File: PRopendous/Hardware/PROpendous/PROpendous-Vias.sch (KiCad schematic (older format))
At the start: 331 parts

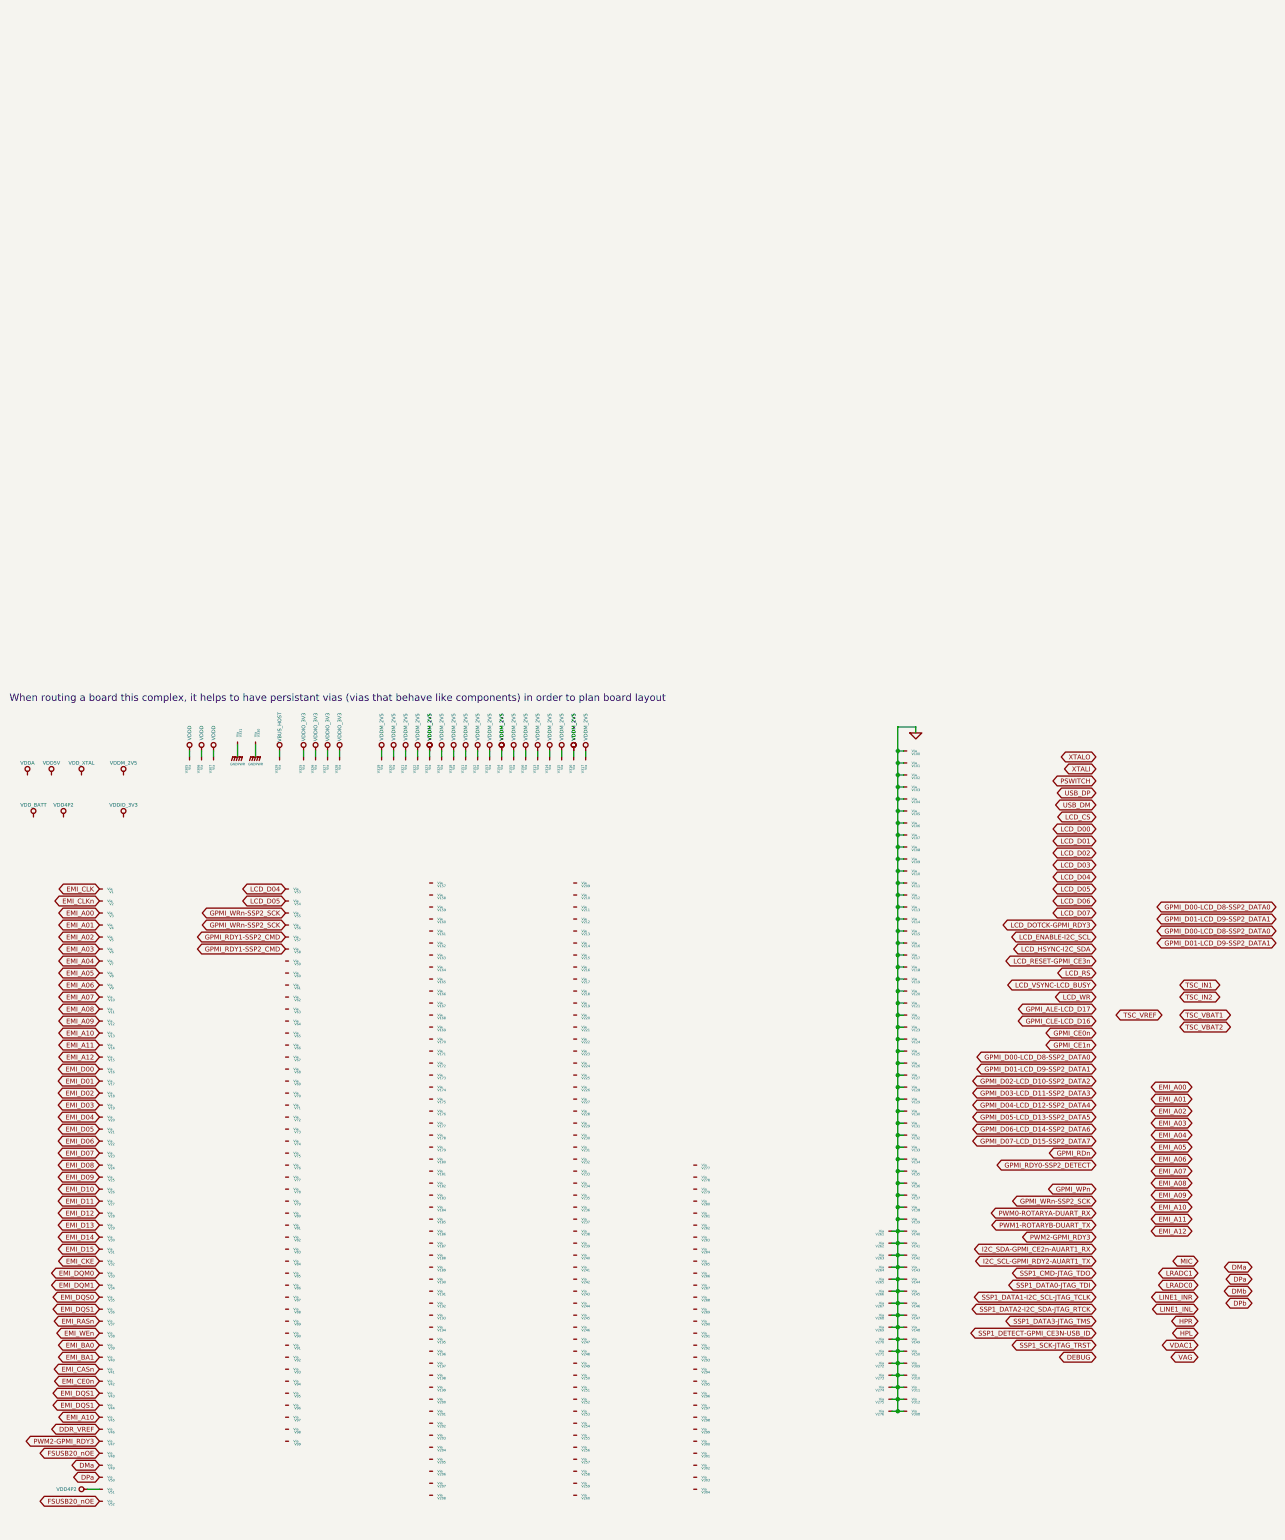
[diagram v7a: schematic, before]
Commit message: First revision of i.MX233-based PROpendous board is complete.
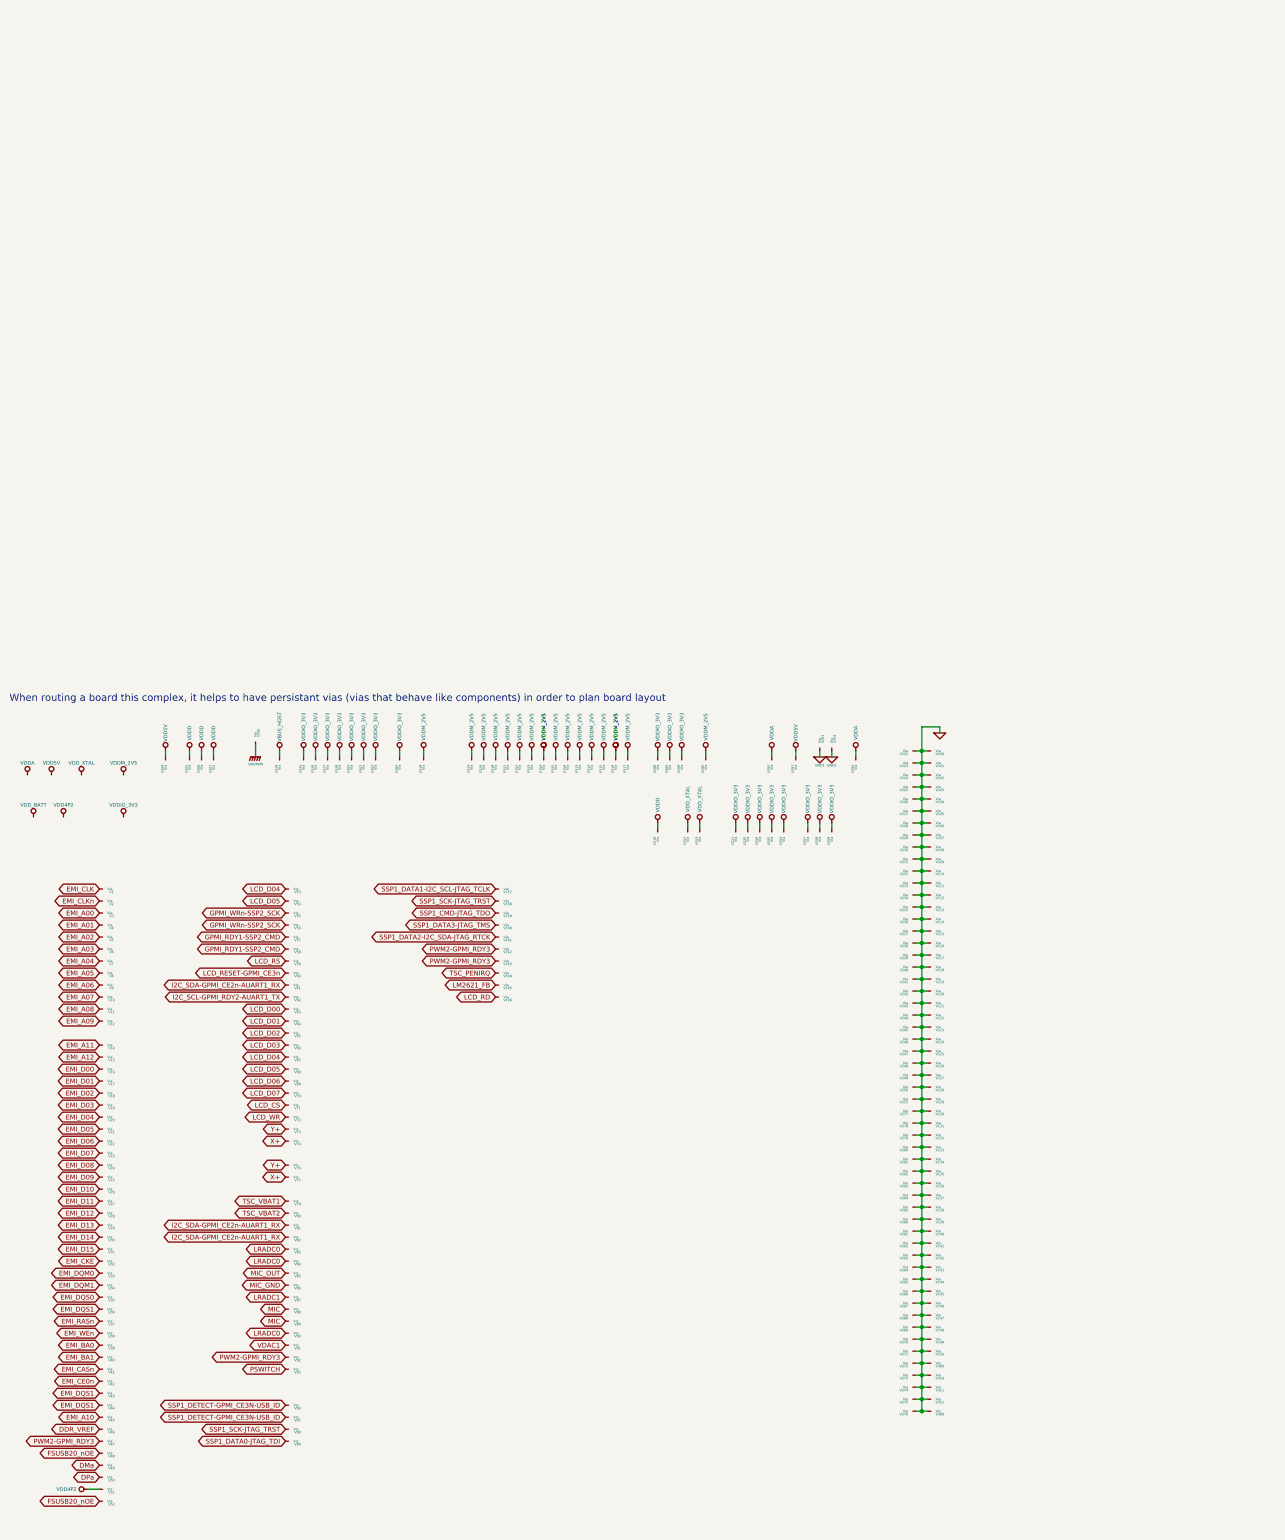
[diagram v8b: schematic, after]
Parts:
- removed V13, V167, V168, V169, V170, V171, V172, V173, V174, V175, V176, V177, V178, V179, V180, V181, V182, V183, V184, V185, V186, V187, V188, V189, V190, V191, V192, V193, V194, V195, V196, V197, V198, V199, V200, V201, V202, V203, V204, V205, V206, V207, V208, V209, V210, V211, V212, V213, V214, V215, V216, V217, V218, V287, V288, V289, V295, V296, V320, V321, V322, V331, V75, V78, V94, V95: VIA, symbol VIA
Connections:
- net GND: now also V222.1 (Via), V223.1 (Via), V224.1 (Via), V225.1 (Via), V226.1 (Via), V227.1 (Via), V228.1 (Via), V229.1 (Via), V230.1 (Via), V231.1 (Via), V232.1 (Via), V233.1 (Via), V234.1 (Via), V235.1 (Via), V236.1 (Via), V237.1 (Via), V238.1 (Via), V239.1 (Via), V240.1 (Via), V241.1 (Via), V242.1 (Via), V243.1 (Via), V244.1 (Via), V245.1 (Via), V246.1 (Via), V247.1 (Via), V248.1 (Via), V249.1 (Via), V250.1 (Via), V251.1 (Via), V277.1 (Via), V278.1 (Via), V279.1 (Via), V280.1 (Via), V281.1 (Via), V282.1 (Via), V283.1 (Via), V284.1 (Via), V285.1 (Via), V286.1 (Via)
- net I2C_SCL-GPMI_RDY2-AUART1_TX: now also V62.1 (Via)
- net I2C_SDA-GPMI_CE2n-AUART1_RX: now also V61.1 (Via), V81.1 (Via), V82.1 (Via)
- net LCD_CS: now also V71.1 (Via)
- net LCD_D00: now also V63.1 (Via)
- net LCD_D01: now also V64.1 (Via)
- net LCD_D02: now also V65.1 (Via)
- net LCD_D03: now also V66.1 (Via)
- net LCD_D04: now also V67.1 (Via)
- net LCD_D05: now also V68.1 (Via)
- net LCD_D06: now also V69.1 (Via)
- net LCD_D07: now also V70.1 (Via)
- net LCD_RESET-GPMI_CE3n: now also V60.1 (Via)
- net LCD_RS: now also V59.1 (Via)
- net LCD_WR: now also V72.1 (Via)
- net LRADC0: now also V83.1 (Via), V84.1 (Via), V90.1 (Via)
- net LRADC1: now also V87.1 (Via)
- net MIC: now also V88.1 (Via), V89.1 (Via)
- net PSWITCH: now also V93.1 (Via)
- net PWM2-GPMI_RDY3: now also V162.1 (Via), V163.1 (Via), V92.1 (Via)
- net SSP1_CMD-JTAG_TDO: now also V159.1 (Via)
- net SSP1_DATA0-JTAG_TDI: now also V99.1 (Via)
- net SSP1_DATA1-I2C_SCL-JTAG_TCLK: now also V157.1 (Via)
- net SSP1_DATA2-I2C_SDA-JTAG_RTCK: now also V161.1 (Via)
- net SSP1_DATA3-JTAG_TMS: now also V160.1 (Via)
- net SSP1_DETECT-GPMI_CE3N-USB_ID: now also V96.1 (Via), V97.1 (Via)
- net SSP1_SCK-JTAG_TRST: now also V158.1 (Via), V98.1 (Via)
- net TSC_VBAT1: now also V79.1 (Via)
- net TSC_VBAT2: now also V80.1 (Via)
- net VDAC1: now also V91.1 (Via)
- net VDD5V: now also V297.1 (Via), V304.1 (Via)
- net VDDA: now also V292.1 (Via), V294.1 (Via)
- net VDDD: now also V219.1 (Via)
- net VDDIO_3V3: now also V220.1 (Via), V221.1 (Via), V254.1 (Via), V255.1 (Via), V256.1 (Via), V257.1 (Via), V258.1 (Via), V259.1 (Via), V260.1 (Via), V298.1 (Via), V299.1 (Via), V300.1 (Via), V301.1 (Via), V302.1 (Via), V303.1 (Via)
- net VDDM_2V5: now also V290.1 (Via)
- net VDD_XTAL: now also V252.1 (Via), V253.1 (Via)
- net MIC_OUT: now reaches V85.1 (Via)
- net MIC_GND: now reaches V86.1 (Via)
- net Y+: now reaches V73.1 (Via)
- net Y+: now also V76.1 (Via)
- net X+: now reaches V74.1 (Via)
- net X+: now also V77.1 (Via)
- net TSC_PENIRQ: now reaches V164.1 (Via)
- net LM2621_FB: now reaches V165.1 (Via)
- net LCD_RD: now reaches V166.1 (Via)
- net GND1: now reaches V293.1 (Via)
- net GND1: now also V291.1 (Via)
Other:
- moved on the sheet: V100, V101, V102, V103, V104, V105, V106, V107, V108, V109, V110, V111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
